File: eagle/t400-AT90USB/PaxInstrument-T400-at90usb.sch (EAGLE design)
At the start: 137 parts, among them IC1 MCP3424, IC2 AT90USB1287-AU, IC3 SN74LVC1G74DCT, J1 MICRO-SDCARD-CONNECTOR-330006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, Q1 DMP2035U-7, Q2 DMP2035U-7, Q3 DMN2075U-7, Q4 DMN2075U-7, Q5 DMP2035U-7, U1 MCP9800, U2 APX809, U3 MCP73831, U4 MIC5219-3.3V, X1 FH12-12S-1S, Y1 RESONATORSMD

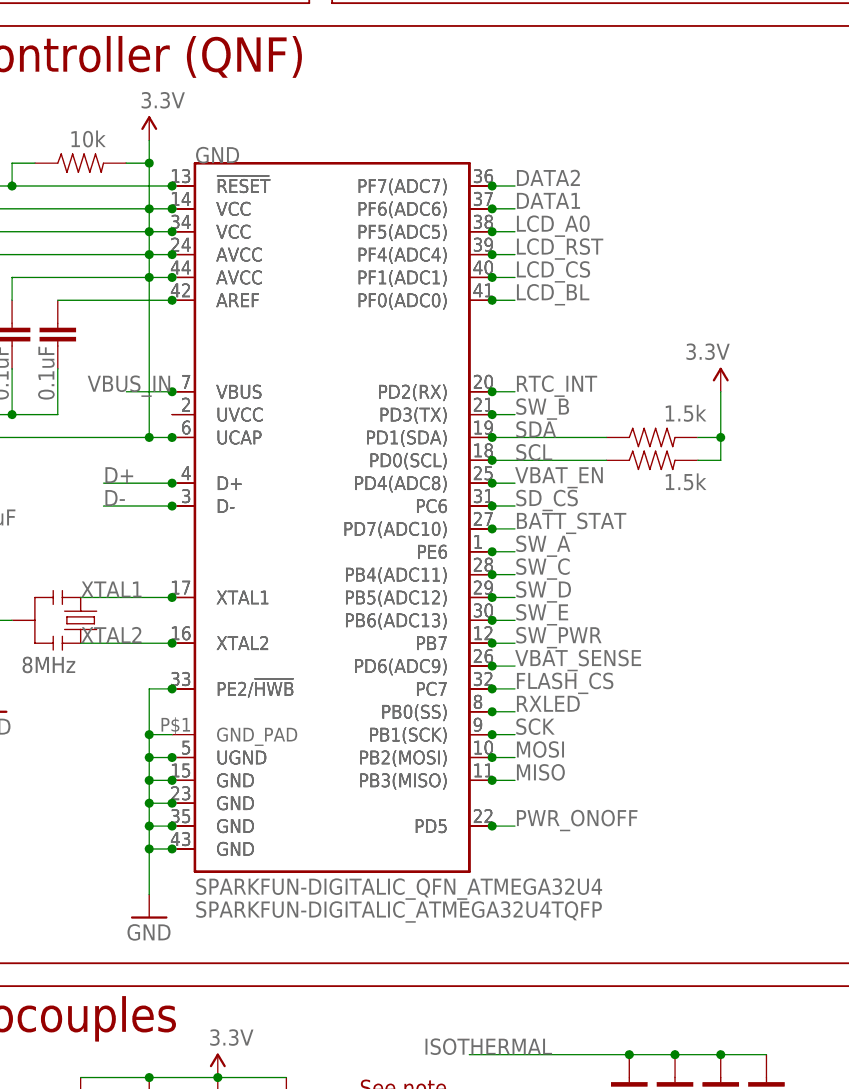
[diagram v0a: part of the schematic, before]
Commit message: Added T400 location PDF. Moved component names on PCB file.
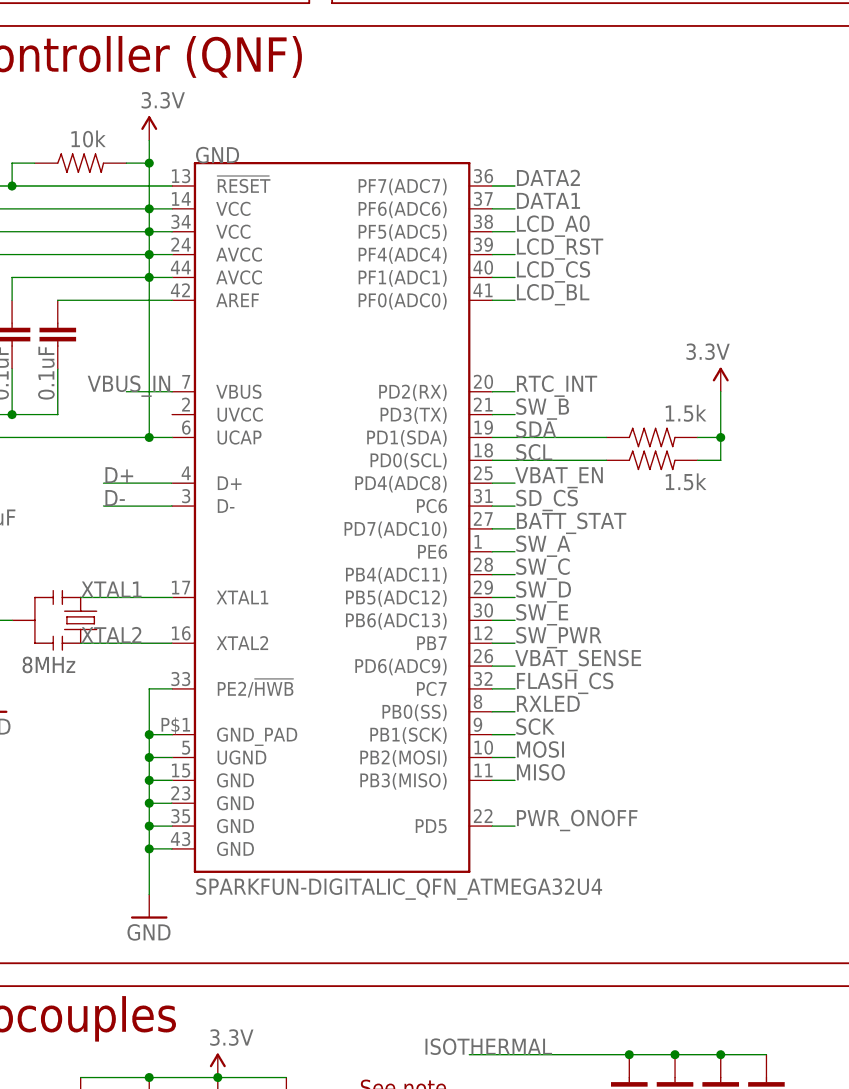
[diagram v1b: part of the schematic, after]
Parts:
- removed U$3: SPARKFUN-DIGITALIC_ATMEGA32U4TQFP, PaxInstrument-T400:SPARKFUN-DIGITALIC_ATMEGA32U4TQFP
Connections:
- removed net N$17: GND.UVCC, U$3.UVCC
- net 3.3V: no longer U$3.AVCC@24, U$3.AVCC@44, U$3.UCAP, U$3.VCC@14, U$3.VCC@34
- net AREF: no longer U$3.AREF
- net BATT_STAT: no longer U$3.PD7(ADC10)
- net D+: no longer U$3.D+
- net D-: no longer U$3.D-
- net DATA1: no longer U$3.PF6(ADC6)
- net DATA2: no longer U$3.PF7(ADC7)
- net FLASH_CS: no longer U$3.PC7
- net GND: no longer U$3.GND@15, U$3.GND@23, U$3.GND@35, U$3.GND@43, U$3.PE2/!HWB, U$3.UGND
- net LCD_A0: no longer U$3.PF5(ADC5)
- net LCD_BL: no longer U$3.PF0(ADC0)
- net LCD_CS: no longer U$3.PF1(ADC1)
- net LCD_RST: no longer U$3.PF4(ADC4)
- net MISO: no longer U$3.PB3(MISO)
- net MOSI: no longer U$3.PB2(MOSI)
- net PWR_ONOFF: no longer U$3.PD5
- net RESET: no longer U$3.!RESET
- net RTC_INT: no longer U$3.PD2(RX)
- net RXLED: no longer U$3.PB0(SS)
- net SCK: no longer U$3.PB1(SCK)
- net SCL: no longer U$3.PD0(SCL)
- net SDA: no longer U$3.PD1(SDA)
- net SD_CS: no longer U$3.PC6
- net SW_A: no longer U$3.PE6
- net SW_B: no longer U$3.PD3(TX)
- net SW_C: no longer U$3.PB4(ADC11)
- net SW_D: no longer U$3.PB5(ADC12)
- net SW_E: no longer U$3.PB6(ADC13)
- net SW_PWR: no longer U$3.PB7
- net VBAT_EN: no longer U$3.PD4(ADC8)
- net VBAT_SENSE: no longer U$3.PD6(ADC9)
- net VBUS_IN: no longer U$3.VBUS
- net XTAL1: no longer U$3.XTAL1
- net XTAL2: no longer U$3.XTAL2
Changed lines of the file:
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@@
 <attribute name="MPN" value="FH12-12S-1SH(55)"/>
-</part>
-<part name="U$3" library="PaxInstrument-T400" deviceset="SPARKFUN-DIGITALIC_ATMEGA32U4" device="TQFP">
-<attribute name="MF" value="Atmel"/>
-<attribute name="MPN" value="ATMEGA32U4-AU"/>
 </part>
 <part name="C21" library="PaxInstrument-T400" deviceset="SPARKFUN-CAPACITORS_CAP" device="0603-CAP" value="0.1uF">
@@
 <attribute name="MF" x="154.94" y="132.08" size="1.778" layer="96" rot="R180" display="off"/>
 </instance>
-<instance part="U$3" gate="G$1" x="63.5" y="139.7" smashed="yes">
-<attribute name="VALUE" x="48.26" y="93.98" size="1.778" layer="96"/>
-<attribute name="MPN" x="63.5" y="139.7" size="1.778" layer="96" display="off"/>
-<attribute name="MF" x="63.5" y="139.7" size="1.778" layer="96" display="off"/>
-</instance>
 <instance part="C21" gate="G$1" x="327.66" y="129.54" smashed="yes" rot="R180">
 <attribute name="VALUE" x="328.041" y="135.636" size="1.778" layer="96" rot="R270"/>
@@
 <junction x="27.94" y="175.26"/>
 <pinref part="GND" gate="G$1" pin="!RESET"/>
-<pinref part="U$3" gate="G$1" pin="!RESET"/>
-<junction x="45.72" y="175.26"/>
 </segment>
 <segment>
@@
 <wire x1="93.98" y1="144.78" x2="81.28" y2="144.78" width="0.1524" layer="91"/>
 <pinref part="GND" gate="G$1" pin="PD0(SCL)"/>
-<pinref part="U$3" gate="G$1" pin="PD0(SCL)"/>
-<junction x="81.28" y="144.78"/>
 </segment>
 <segment>
@@
 <wire x1="93.98" y1="147.32" x2="81.28" y2="147.32" width="0.1524" layer="91"/>
 <pinref part="GND" gate="G$1" pin="PD1(SDA)"/>
-<pinref part="U$3" gate="G$1" pin="PD1(SDA)"/>
-<junction x="81.28" y="147.32"/>
 </segment>
 <segment>
@@
 <pinref part="GND" gate="G$1" pin="AVCC@24"/>
 <wire x1="45.72" y1="167.64" x2="43.18" y2="167.64" width="0.1524" layer="91"/>
-<pinref part="U$3" gate="G$1" pin="AVCC@24"/>
-<junction x="45.72" y="167.64"/>
-<pinref part="U$3" gate="G$1" pin="AVCC@44"/>
-<junction x="45.72" y="165.1"/>
-<pinref part="U$3" gate="G$1" pin="UCAP"/>
-<junction x="45.72" y="147.32"/>
-<pinref part="U$3" gate="G$1" pin="VCC@14"/>
-<junction x="45.72" y="172.72"/>
-<pinref part="U$3" gate="G$1" pin="VCC@34"/>
-<junction x="45.72" y="170.18"/>
 </segment>
 <segment>
@@
 <wire x1="45.72" y1="114.3" x2="43.18" y2="114.3" width="0.1524" layer="91"/>
 <junction x="43.18" y="114.3"/>
-<pinref part="U$3" gate="G$1" pin="GND@15"/>
-<junction x="45.72" y="109.22"/>
-<pinref part="U$3" gate="G$1" pin="GND@23"/>
-<junction x="45.72" y="106.68"/>
-<pinref part="U$3" gate="G$1" pin="GND@35"/>
-<junction x="45.72" y="104.14"/>
-<pinref part="U$3" gate="G$1" pin="GND@43"/>
-<junction x="45.72" y="101.6"/>
-<pinref part="U$3" gate="G$1" pin="PE2/!HWB"/>
-<junction x="45.72" y="119.38"/>
-<pinref part="U$3" gate="G$1" pin="UGND"/>
-<junction x="45.72" y="111.76"/>
 </segment>
 <segment>
@@
 <label x="38.1" y="139.7" size="1.778" layer="95"/>
 <pinref part="GND" gate="G$1" pin="D-"/>
-<pinref part="U$3" gate="G$1" pin="D-"/>
-<junction x="45.72" y="139.7"/>
 </segment>
 <segment>
@@
 <label x="38.1" y="142.24" size="1.778" layer="95"/>
 <pinref part="GND" gate="G$1" pin="D+"/>
-<pinref part="U$3" gate="G$1" pin="D+"/>
-<junction x="45.72" y="142.24"/>
 </segment>
 <segment>
@@
 <label x="83.82" y="109.22" size="1.778" layer="95"/>
 <pinref part="GND" gate="G$1" pin="PB3(MISO)"/>
-<pinref part="U$3" gate="G$1" pin="PB3(MISO)"/>
-<junction x="81.28" y="109.22"/>
 </segment>
 <segment>
@@
 <label x="83.82" y="111.76" size="1.778" layer="95"/>
 <pinref part="GND" gate="G$1" pin="PB2(MOSI)"/>
-<pinref part="U$3" gate="G$1" pin="PB2(MOSI)"/>
-<junction x="81.28" y="111.76"/>
 </segment>
 <segment>
@@
 <label x="83.82" y="114.3" size="1.778" layer="95"/>
 <pinref part="GND" gate="G$1" pin="PB1(SCK)"/>
-<pinref part="U$3" gate="G$1" pin="PB1(SCK)"/>
-<junction x="81.28" y="114.3"/>
 </segment>
 <segment>
@@
 <label x="35.56" y="129.54" size="1.778" layer="95"/>
 <pinref part="GND" gate="G$1" pin="XTAL1"/>
-<pinref part="U$3" gate="G$1" pin="XTAL1"/>
-<junction x="45.72" y="129.54"/>
 </segment>
 <segment>
@@
 <label x="35.56" y="124.46" size="1.778" layer="95"/>
 <pinref part="GND" gate="G$1" pin="XTAL2"/>
-<pinref part="U$3" gate="G$1" pin="XTAL2"/>
-<junction x="45.72" y="124.46"/>
 </segment>
 <segment>
@@
 <label x="83.82" y="162.56" size="1.778" layer="95"/>
 <pinref part="GND" gate="G$1" pin="PF0(ADC0)"/>
-<pinref part="U$3" gate="G$1" pin="PF0(ADC0)"/>
-<junction x="81.28" y="162.56"/>
 </segment>
 <segment>
@@
 <label x="83.82" y="170.18" size="1.778" layer="95"/>
 <pinref part="GND" gate="G$1" pin="PF5(ADC5)"/>
-<pinref part="U$3" gate="G$1" pin="PF5(ADC5)"/>
-<junction x="81.28" y="170.18"/>
 </segment>
 <segment>
@@
 <label x="83.82" y="165.1" size="1.778" layer="95"/>
 <pinref part="GND" gate="G$1" pin="PF1(ADC1)"/>
-<pinref part="U$3" gate="G$1" pin="PF1(ADC1)"/>
-<junction x="81.28" y="165.1"/>
 </segment>
 <segment>
@@
 <label x="83.82" y="167.64" size="1.778" layer="95"/>
 <pinref part="GND" gate="G$1" pin="PF4(ADC4)"/>
-<pinref part="U$3" gate="G$1" pin="PF4(ADC4)"/>
-<junction x="81.28" y="167.64"/>
 </segment>
 <segment>
@@
 <label x="83.82" y="139.7" size="1.778" layer="95"/>
 <pinref part="GND" gate="G$1" pin="PC6"/>
-<pinref part="U$3" gate="G$1" pin="PC6"/>
-<junction x="81.28" y="139.7"/>
 </segment>
 <segment>
@@
 <label x="83.82" y="104.14" size="1.778" layer="95"/>
 <pinref part="GND" gate="G$1" pin="PD5"/>
-<pinref part="U$3" gate="G$1" pin="PD5"/>
-<junction x="81.28" y="104.14"/>
 </segment>
 <segment>
@@
 <label x="83.82" y="127" size="1.778" layer="95"/>
 <pinref part="GND" gate="G$1" pin="PB6(ADC13)"/>
-<pinref part="U$3" gate="G$1" pin="PB6(ADC13)"/>
-<junction x="81.28" y="127"/>
 </segment>
 <segment>
@@
 <label x="83.82" y="129.54" size="1.778" layer="95"/>
 <pinref part="GND" gate="G$1" pin="PB5(ADC12)"/>
-<pinref part="U$3" gate="G$1" pin="PB5(ADC12)"/>
-<junction x="81.28" y="129.54"/>
 </segment>
 <segment>
@@
 <label x="83.82" y="149.86" size="1.778" layer="95"/>
 <pinref part="GND" gate="G$1" pin="PD3(TX)"/>
-<pinref part="U$3" gate="G$1" pin="PD3(TX)"/>
-<junction x="81.28" y="149.86"/>
 </segment>
 <segment>
@@
 <label x="83.82" y="132.08" size="1.778" layer="95"/>
 <pinref part="GND" gate="G$1" pin="PB4(ADC11)"/>
-<pinref part="U$3" gate="G$1" pin="PB4(ADC11)"/>
-<junction x="81.28" y="132.08"/>
 </segment>
 <segment>
@@
 <label x="83.82" y="134.62" size="1.778" layer="95"/>
 <pinref part="GND" gate="G$1" pin="PE6"/>
-<pinref part="U$3" gate="G$1" pin="PE6"/>
-<junction x="81.28" y="134.62"/>
 </segment>
 <segment>
@@
 <label x="83.82" y="137.16" size="1.778" layer="95"/>
 <pinref part="GND" gate="G$1" pin="PD7(ADC10)"/>
-<pinref part="U$3" gate="G$1" pin="PD7(ADC10)"/>
-<junction x="81.28" y="137.16"/>
 </segment>
 <segment>
@@
 <label x="83.82" y="124.46" size="1.778" layer="95"/>
 <pinref part="GND" gate="G$1" pin="PB7"/>
-<pinref part="U$3" gate="G$1" pin="PB7"/>
-<junction x="81.28" y="124.46"/>
 </segment>
 <segment>
@@
 <label x="83.82" y="121.92" size="1.778" layer="95"/>
 <pinref part="GND" gate="G$1" pin="PD6(ADC9)"/>
-<pinref part="U$3" gate="G$1" pin="PD6(ADC9)"/>
-<junction x="81.28" y="121.92"/>
 </segment>
 <segment>
@@
 <label x="83.82" y="152.4" size="1.778" layer="95"/>
 <pinref part="GND" gate="G$1" pin="PD2(RX)"/>
-<pinref part="U$3" gate="G$1" pin="PD2(RX)"/>
-<junction x="81.28" y="152.4"/>
 </segment>
 <segment>
@@
 <wire x1="45.72" y1="152.4" x2="40.64" y2="152.4" width="0.1524" layer="91"/>
 <pinref part="GND" gate="G$1" pin="VBUS"/>
-<pinref part="U$3" gate="G$1" pin="VBUS"/>
-<junction x="45.72" y="152.4"/>
 </segment>
 <segment>
@@
 <label x="83.82" y="142.24" size="1.778" layer="95"/>
 <pinref part="GND" gate="G$1" pin="PD4(ADC8)"/>
-<pinref part="U$3" gate="G$1" pin="PD4(ADC8)"/>
-<junction x="81.28" y="142.24"/>
 </segment>
 <segment>
@@
 <label x="83.82" y="119.38" size="1.778" layer="95"/>
 <pinref part="GND" gate="G$1" pin="PC7"/>
-<pinref part="U$3" gate="G$1" pin="PC7"/>
-<junction x="81.28" y="119.38"/>
 </segment>
 <segment>
@@
 <pinref part="C3" gate="G$1" pin="1"/>
 <wire x1="33.02" y1="162.56" x2="45.72" y2="162.56" width="0.1524" layer="91"/>
-<pinref part="U$3" gate="G$1" pin="AREF"/>
-<junction x="45.72" y="162.56"/>
 </segment>
 <segment>
@@
 <label x="83.82" y="175.26" size="1.778" layer="95"/>
 <pinref part="GND" gate="G$1" pin="PF7(ADC7)"/>
-<pinref part="U$3" gate="G$1" pin="PF7(ADC7)"/>
-<junction x="81.28" y="175.26"/>
 </segment>
 <segment>
@@
 <wire x1="-83.82" y1="99.06" x2="-86.36" y2="99.06" width="0.1524" layer="91"/>
 <label x="-86.36" y="99.06" size="1.778" layer="95" rot="MR0"/>
-</segment>
-</net>
-<net name="N$17" class="0">
-<segment>
-<pinref part="GND" gate="G$1" pin="UVCC"/>
-<pinref part="U$3" gate="G$1" pin="UVCC"/>
 </segment>
 </net>
@@
 <label x="83.82" y="116.84" size="1.778" layer="95"/>
 <pinref part="GND" gate="G$1" pin="PB0(SS)"/>
-<pinref part="U$3" gate="G$1" pin="PB0(SS)"/>
-<junction x="81.28" y="116.84"/>
 </segment>
 <segment>
@@
 <label x="83.82" y="172.72" size="1.778" layer="95"/>
 <pinref part="GND" gate="G$1" pin="PF6(ADC6)"/>
-<pinref part="U$3" gate="G$1" pin="PF6(ADC6)"/>
-<junction x="81.28" y="172.72"/>
-</segment>
-<segment>
+</segment>
+<segment>
